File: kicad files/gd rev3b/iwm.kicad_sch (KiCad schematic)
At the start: 28 parts, among them J2 DB19_4, J3 DB19_16, J4 EN, J5 DSUB19, J6 FDC Hdr, J7 EN, J8 EN, Q8 BC817, Q9 BC817, U11 IWM

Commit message: Schematic changes for #52, #50, #70, #51, #61, #69, #71
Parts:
- removed Q8, Q9: BC817, Package_TO_SOT_SMD:SOT-23, symbol Mega IIe Rev3 Symbols:Q_NPN_BEC
- added Q8, Q9: MMBT3906, Package_TO_SOT_SMD:SOT-23, symbol Transistor_BJT:MMBT3906
- R19, R75: value 470 -> 1k
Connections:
- net +5V: now also Q8.2 (E), Q9.2 (E); no longer R19.1, R75.1
- net GND: now also D16.1 (K), D3.1 (K)
- net at R77.2: now also Q9.1 (B)
- net at R76.2: now also Q8.1 (B)
- new net: Q9.3 (C), R75.1
- new net: Q8.3 (C), R19.1
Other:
- moved on the sheet: D16, D3, R19, R75, R76, R77

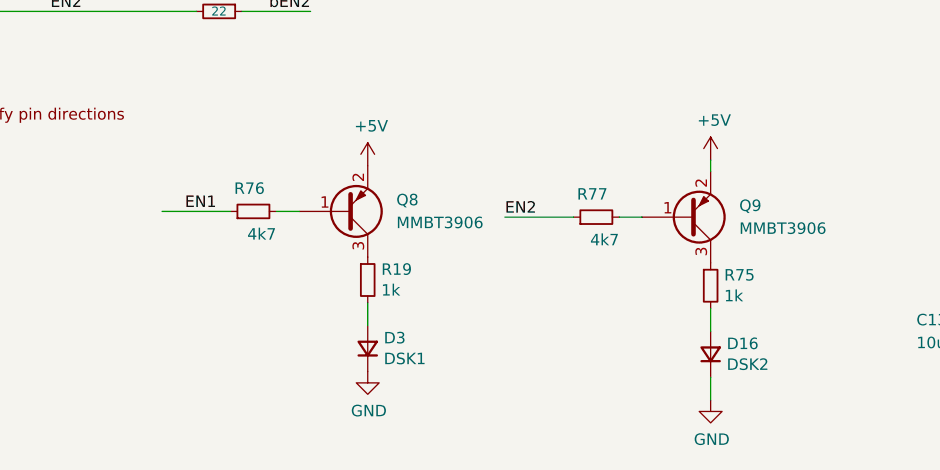
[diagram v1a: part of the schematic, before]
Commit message: placed IWM EN Qs, but need to fix 5V for them
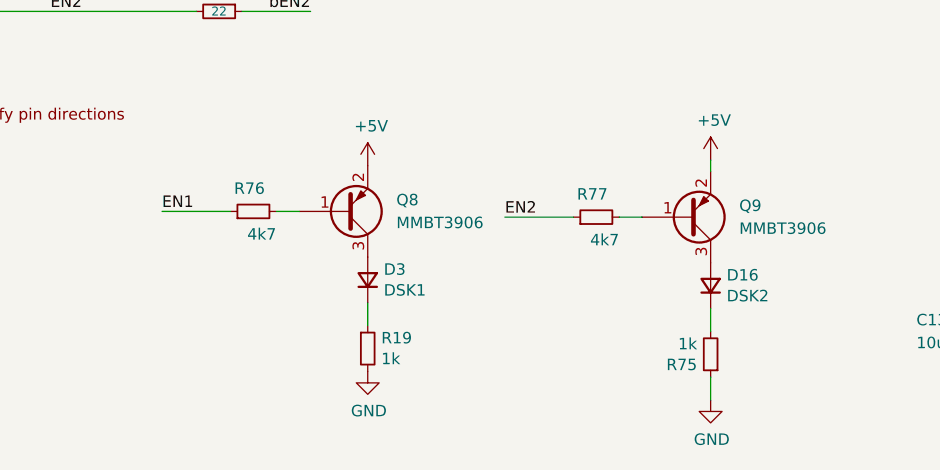
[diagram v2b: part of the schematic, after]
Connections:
- net GND: now also R19.2, R75.1; no longer D16.1 (K), D3.1 (K)
- net at Q9.3 (C): now also D16.2 (A); no longer R75.1
- net at R19.1: now also D3.1 (K); no longer Q8.3 (C)
- net at D3.2 (A): now also Q8.3 (C); no longer R19.2
- net at R75.2: now also D16.1 (K); no longer D16.2 (A)
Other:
- moved on the sheet: D16, D3, R19, R75
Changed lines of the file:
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@@
     (effects (font (size 1.27 1.27)) (justify right bottom))
   )
-  (label "EN1" (at 129.54 135.255 0) (fields_autoplaced)
+  (label "EN1" (at 127 135.255 0) (fields_autoplaced)
     (effects (font (size 1.27 1.27)) (justify left bottom))
   )
@@
     )
   )
-  (symbol (lib_name "R_0805_5") (lib_id "Mega IIe Rev3 Symbols:R_0805_5") (at 149.86 142.875 0) (unit 1)
-    (in_bom yes) (on_board yes) (dnp no)
-    (property "Reference" "R19" (at 151.3586 141.7066 0)
-      (effects (font (size 1.27 1.27)) (justify left))
-    )
-    (property "Value" "1k" (at 151.3586 144.018 0)
-      (effects (font (size 1.27 1.27)) (justify left))
-    )
-    (property "Footprint" "Resistor_SMD:R_0805_2012Metric" (at 149.86 142.875 0)
-      (effects (font (size 1.27 1.27)) hide)
-    )
-    (property "Datasheet" "~" (at 149.86 142.875 0)
+  (symbol (lib_name "R_0805_5") (lib_id "Mega IIe Rev3 Symbols:R_0805_5") (at 149.86 150.495 0) (unit 1)
+    (in_bom yes) (on_board yes) (dnp no)
+    (property "Reference" "R19" (at 151.3586 149.3266 0)
+      (effects (font (size 1.27 1.27)) (justify left))
+    )
+    (property "Value" "1k" (at 151.3586 151.638 0)
+      (effects (font (size 1.27 1.27)) (justify left))
+    )
+    (property "Footprint" "Resistor_SMD:R_0805_2012Metric" (at 149.86 150.495 0)
+      (effects (font (size 1.27 1.27)) hide)
+    )
+    (property "Datasheet" "~" (at 149.86 150.495 0)
       (effects (font (size 1.27 1.27)) hide)
     )
@@
     )
   )
-  (symbol (lib_id "Mega IIe Rev3 Symbols:D_1206") (at 187.96 151.13 90) (unit 1)
-    (in_bom yes) (on_board yes) (dnp no)
-    (property "Reference" "D16" (at 189.738 149.9616 90)
+  (symbol (lib_id "Mega IIe Rev3 Symbols:D_1206") (at 187.96 143.51 90) (unit 1)
+    (in_bom yes) (on_board yes) (dnp no)
+    (property "Reference" "D16" (at 189.738 142.3416 90)
       (effects (font (size 1.27 1.27)) (justify right))
     )
-    (property "Value" "DSK2" (at 189.738 152.273 90)
+    (property "Value" "DSK2" (at 189.738 144.653 90)
       (effects (font (size 1.27 1.27)) (justify right))
     )
-    (property "Footprint" "LED_SMD:LED_1206_3216Metric" (at 187.96 151.13 90)
-      (effects (font (size 1.27 1.27)) hide)
-    )
-    (property "Datasheet" "~" (at 187.96 151.13 90)
+    (property "Footprint" "LED_SMD:LED_1206_3216Metric" (at 187.96 143.51 90)
+      (effects (font (size 1.27 1.27)) hide)
+    )
+    (property "Datasheet" "~" (at 187.96 143.51 90)
       (effects (font (size 1.27 1.27)) hide)
     )
@@
     )
   )
-  (symbol (lib_name "R_0805_5") (lib_id "Mega IIe Rev3 Symbols:R_0805_5") (at 187.96 143.51 0) (unit 1)
-    (in_bom yes) (on_board yes) (dnp no)
-    (property "Reference" "R75" (at 189.4586 142.3416 0)
-      (effects (font (size 1.27 1.27)) (justify left))
-    )
-    (property "Value" "1k" (at 189.4586 144.653 0)
-      (effects (font (size 1.27 1.27)) (justify left))
-    )
-    (property "Footprint" "Resistor_SMD:R_0805_2012Metric" (at 187.96 143.51 0)
-      (effects (font (size 1.27 1.27)) hide)
-    )
-    (property "Datasheet" "~" (at 187.96 143.51 0)
+  (symbol (lib_name "R_0805_5") (lib_id "Mega IIe Rev3 Symbols:R_0805_5") (at 187.96 151.13 180) (unit 1)
+    (in_bom yes) (on_board yes) (dnp no)
+    (property "Reference" "R75" (at 186.4614 152.2984 0)
+      (effects (font (size 1.27 1.27)) (justify left))
+    )
+    (property "Value" "1k" (at 186.4614 149.987 0)
+      (effects (font (size 1.27 1.27)) (justify left))
+    )
+    (property "Footprint" "Resistor_SMD:R_0805_2012Metric" (at 187.96 151.13 0)
+      (effects (font (size 1.27 1.27)) hide)
+    )
+    (property "Datasheet" "~" (at 187.96 151.13 0)
       (effects (font (size 1.27 1.27)) hide)
     )
@@
     )
   )
-  (symbol (lib_id "Mega IIe Rev3 Symbols:D_1206") (at 149.86 150.495 90) (unit 1)
-    (in_bom yes) (on_board yes) (dnp no)
-    (property "Reference" "D3" (at 151.638 149.3266 90)
+  (symbol (lib_id "Mega IIe Rev3 Symbols:D_1206") (at 149.86 142.875 90) (unit 1)
+    (in_bom yes) (on_board yes) (dnp no)
+    (property "Reference" "D3" (at 151.638 141.7066 90)
       (effects (font (size 1.27 1.27)) (justify right))
     )
-    (property "Value" "DSK1" (at 151.638 151.638 90)
+    (property "Value" "DSK1" (at 151.638 144.018 90)
       (effects (font (size 1.27 1.27)) (justify right))
     )
-    (property "Footprint" "LED_SMD:LED_1206_3216Metric" (at 149.86 150.495 90)
-      (effects (font (size 1.27 1.27)) hide)
-    )
-    (property "Datasheet" "~" (at 149.86 150.495 90)
-      (effects (font (size 1.27 1.27)) hide)
-    )
+    (property "Footprint" "LED_SMD:LED_1206_3216Metric" (at 149.86 142.875 90)
+      (effects (font (size 1.27 1.27)) hide)
+    )
+    (property "Datasheet" "~" (at 149.86 142.875 90)
+      (effects (font (size 1.27 1.27)) hide)
+    )

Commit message: rev 3b is ready for fab
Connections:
- net +5V: now also J3.1 (Pin_1)
- net DB19-16: now also J3.2 (Pin_2); no longer J3.1 (Pin_1)
- net GND: no longer J3.2 (Pin_2)
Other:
- moved on the sheet: J3
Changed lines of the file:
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@@
-    (stroke (width 0) (type default))
-  )
-  (wire (pts (xy 175.26 67.31) (xy 175.26 68.58))
     (stroke (width 0) (type default))
   )
@@
     (stroke (width 0) (type default))
   )
-  (wire (pts (xy 173.99 64.77) (xy 182.88 64.77))
+  (wire (pts (xy 173.99 74.295) (xy 184.785 74.295))
     (stroke (width 0) (type default))
   )
@@
     (stroke (width 0) (type default))
   )
+  (wire (pts (xy 173.99 71.755) (xy 175.26 71.755))
+    (stroke (width 0) (type default))
+  )
   (wire (pts (xy 224.79 151.13) (xy 224.79 152.4))
     (stroke (width 0) (type default))
@@
     (stroke (width 0) (type default))
   )
+  (wire (pts (xy 175.26 69.85) (xy 175.26 71.755))
+    (stroke (width 0) (type default))
+  )
   (wire (pts (xy 82.55 85.09) (xy 73.66 85.09))
     (stroke (width 0) (type default))
@@
   )
   (wire (pts (xy 224.79 110.49) (xy 232.41 110.49))
-    (stroke (width 0) (type default))
-  )
-  (wire (pts (xy 173.99 67.31) (xy 175.26 67.31))
     (stroke (width 0) (type default))
   )
@@
     (effects (font (size 1.27 1.27)) (justify right bottom))
   )
-  (label "DB19-16" (at 182.88 64.77 180) (fields_autoplaced)
+  (label "DB19-16" (at 184.785 74.295 180) (fields_autoplaced)
     (effects (font (size 1.27 1.27)) (justify right bottom))
   )
@@
         (path "/e63e39d7-6ac0-4ffd-8aa3-1841a4541b55/a9c8f5ac-a28a-4770-a319-78cb5bb789be"
           (reference "#PWR0191") (unit 1)
+        )
+      )
+    )
+  )
+  (symbol (lib_id "power:+5V") (at 175.26 69.85 0) (unit 1)
+    (in_bom yes) (on_board yes) (dnp no)
+    (property "Reference" "#PWR020" (at 175.26 73.66 0)
+      (effects (font (size 1.27 1.27)) hide)
+    )
+    (property "Value" "+5V" (at 175.641 65.4558 0)
+      (effects (font (size 1.27 1.27)))
+    )
+    (property "Footprint" "" (at 175.26 69.85 0)
+      (effects (font (size 1.27 1.27)) hide)
+    )
+    (property "Datasheet" "" (at 175.26 69.85 0)
+      (effects (font (size 1.27 1.27)) hide)
+    )
+    (pin "1")
+    (instances
+      (project "gd rev3b"
+        (path "/e63e39d7-6ac0-4ffd-8aa3-1841a4541b55/a9c8f5ac-a28a-4770-a319-78cb5bb789be"
+          (reference "#PWR020") (unit 1)
         )
       )
@@
   (symbol (lib_id "Mega IIe Rev3 Symbols:Conn_01x19") (at 217.17 48.26 90) (unit 1)
     (in_bom yes) (on_board yes) (dnp no)
-    (property "Reference" "J5" (at 211.6582 48.1584 90)
+    (property "Reference" "J5" (at 213.36 42.545 90)
       (effects (font (size 1.27 1.27)))
     )
@@
     )
   )
-  (symbol (lib_id "Mega IIe Rev3 Symbols:Conn_01x02") (at 168.91 64.77 0) (mirror y) (unit 1)
-    (in_bom yes) (on_board yes) (dnp no)
-    (property "Reference" "J3" (at 170.9928 59.2582 0)
-      (effects (font (size 1.27 1.27)))
-    )
-    (property "Value" "DB19_16" (at 170.9928 61.5696 0)
-      (effects (font (size 1.27 1.27)))
-    )
-    (property "Footprint" "My Libraries:PinHeader_1x02_P2.54mm_Vertical-LOCK" (at 168.91 64.77 0)
-      (effects (font (size 1.27 1.27)) hide)
-    )
-    (property "Datasheet" "~" (at 168.91 64.77 0)
+  (symbol (lib_id "Mega IIe Rev3 Symbols:Conn_01x02") (at 168.91 71.755 0) (mirror y) (unit 1)
+    (in_bom yes) (on_board yes) (dnp no)
+    (property "Reference" "J3" (at 165.1 72.39 0)
+      (effects (font (size 1.27 1.27)))
+    )
+    (property "Value" "DB19_16" (at 162.56 74.93 0)
+      (effects (font (size 1.27 1.27)))
+    )
+    (property "Footprint" "My Libraries:PinHeader_1x02_P2.54mm_Vertical-LOCK" (at 168.91 71.755 0)
+      (effects (font (size 1.27 1.27)) hide)
+    )
+    (property "Datasheet" "~" (at 168.91 71.755 0)
       (effects (font (size 1.27 1.27)) hide)
     )
@@
         )
       )
-    )
-  )
-  (symbol (lib_id "power:GND") (at 175.26 68.58 0) (unit 1)
-    (in_bom yes) (on_board yes) (dnp no)
-    (property "Reference" "#PWR0171" (at 175.26 74.93 0)
-      (effects (font (size 1.27 1.27)) hide)
-    )
-    (property "Value" "GND" (at 175.387 72.9742 0)
-      (effects (font (size 1.27 1.27)))
-    )
-    (property "Footprint" "" (at 175.26 68.58 0)
-      (effects (font (size 1.27 1.27)) hide)
-    )
-    (property "Datasheet" "" (at 175.26 68.58 0)
-      (effects (font (size 1.27 1.27)) hide)
-    )
-    (pin "1")
-    (instances
-      (project "gd rev3b"
-        (path "/e63e39d7-6ac0-4ffd-8aa3-1841a4541b55/a9c8f5ac-a28a-4770-a319-78cb5bb789be"
-          (reference "#PWR0171") (unit 1)
-        )
-      )
